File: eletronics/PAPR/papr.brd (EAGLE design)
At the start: 44.4 x 37.8 mm, 7 parts

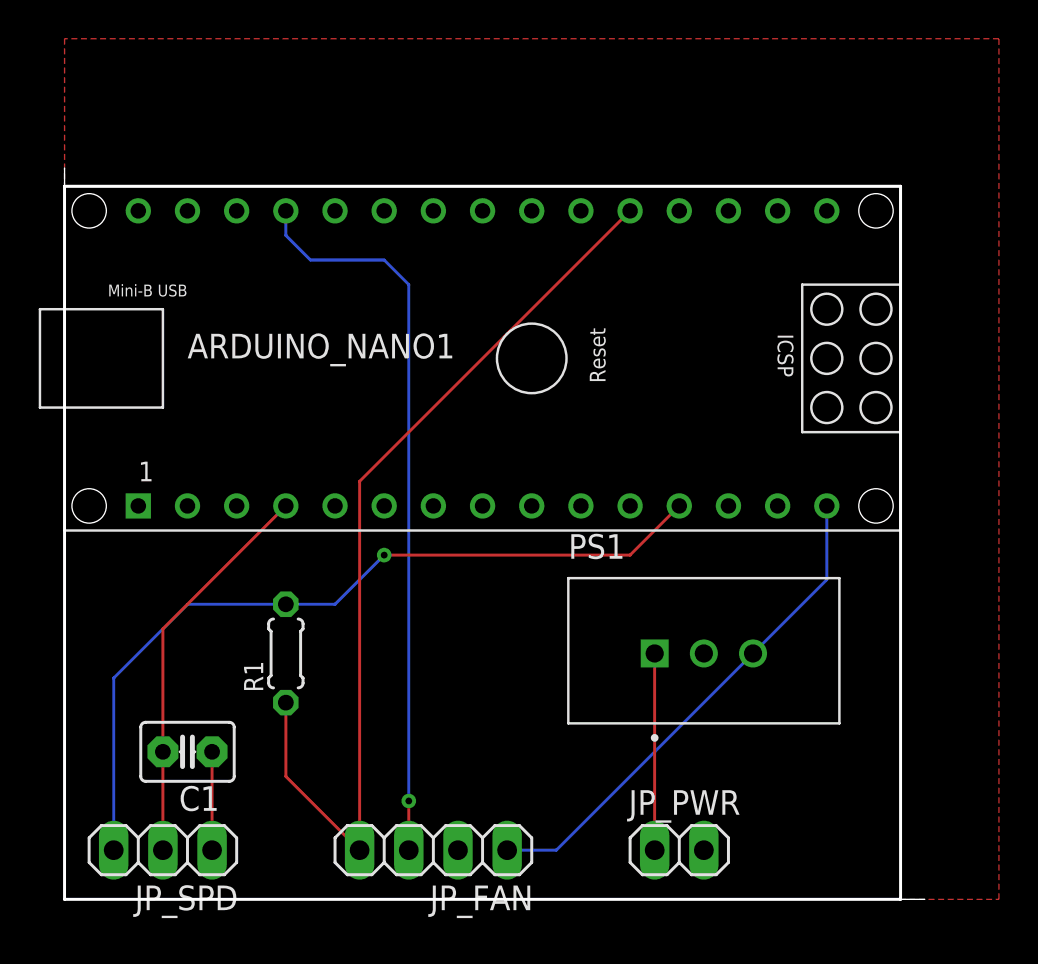
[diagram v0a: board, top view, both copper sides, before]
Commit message: Routed fan pwm solely on the bottom layer, had pointless short top trace
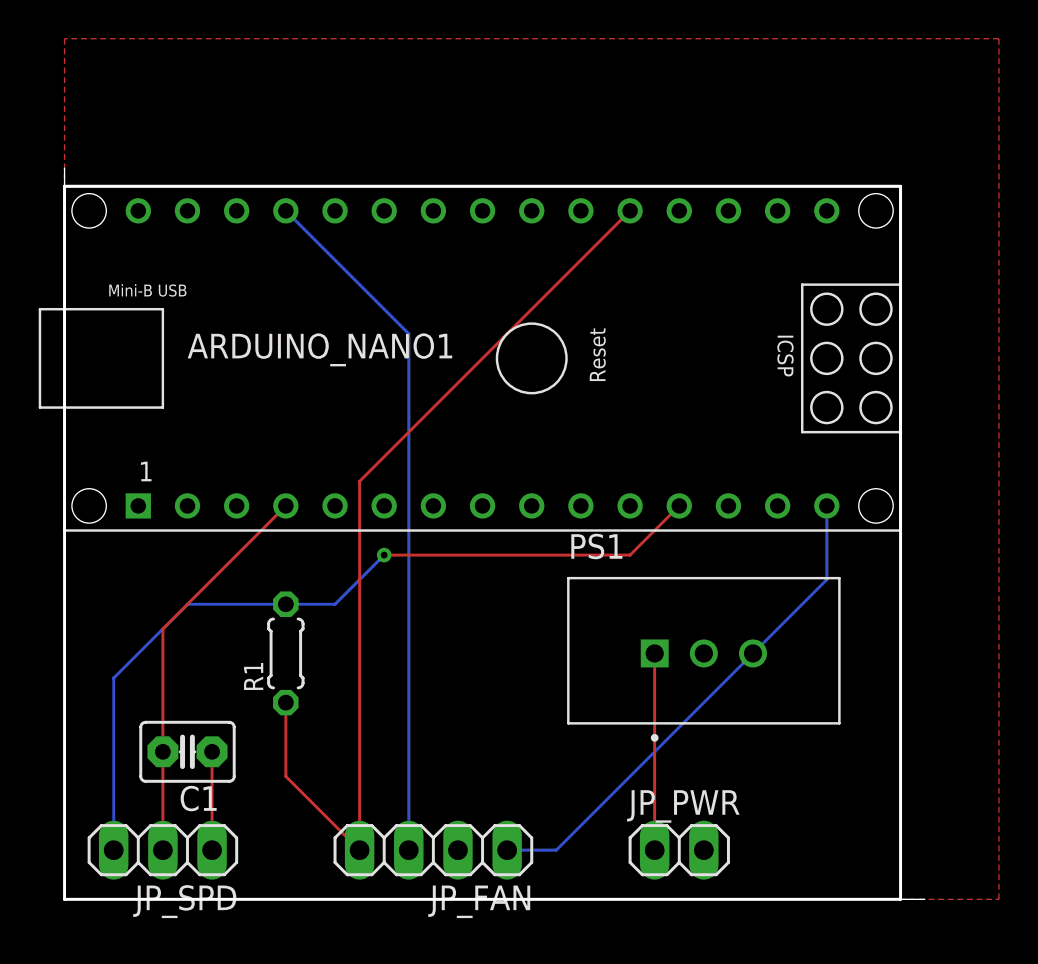
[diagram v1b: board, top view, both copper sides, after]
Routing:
- net FAN_PWM: track 37.9 -> 35.7 mm, vias 1 -> 0
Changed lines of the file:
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@@
 <contactref element="ARDUINO_NANO1" pad="27"/>
 <contactref element="JP_FAN" pad="3"/>
-<wire x1="17.78" y1="2.54" x2="17.78" y2="5.08" width="0.1524" layer="1"/>
-<via x="17.78" y="5.08" extent="1-16" drill="0.35"/>
-<wire x1="17.78" y1="5.08" x2="17.78" y2="31.75" width="0.1524" layer="16"/>
-<wire x1="17.78" y1="31.75" x2="16.51" y2="33.02" width="0.1524" layer="16"/>
-<wire x1="16.51" y1="33.02" x2="12.7" y2="33.02" width="0.1524" layer="16"/>
-<wire x1="12.7" y1="33.02" x2="11.43" y2="34.29" width="0.1524" layer="16"/>
-<wire x1="11.43" y1="34.29" x2="11.43" y2="35.56" width="0.1524" layer="16"/>
+<wire x1="17.78" y1="2.54" x2="17.78" y2="29.21" width="0.1524" layer="16"/>
+<wire x1="17.78" y1="29.21" x2="11.43" y2="35.56" width="0.1524" layer="16"/>
 </signal>
 <signal name="SPEED_IN">
